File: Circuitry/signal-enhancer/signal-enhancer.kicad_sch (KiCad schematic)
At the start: 25 parts, among them J1 Conn_01x06_Pin, J2 Conn_01x06_Pin, U1 NE555P, U2 74HC14, U4 SN74LS74AN, U5 SN74LS74AN, U7 SN74LS74AN

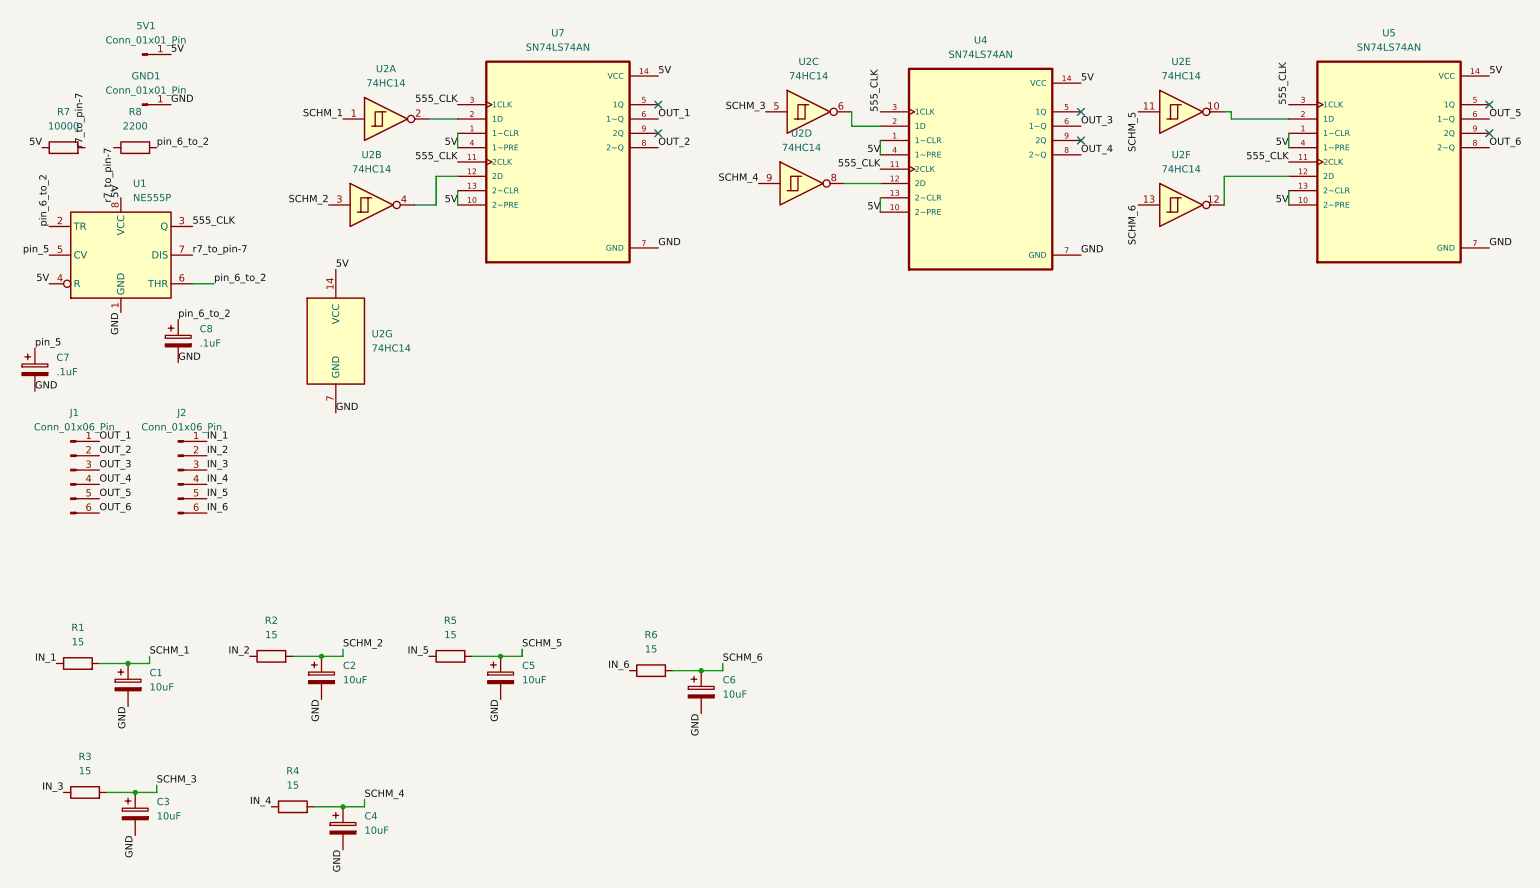
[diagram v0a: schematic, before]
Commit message: Update PCB layout and connector footprints
Modified component values to include Ω symbols and moved value layers to F.SilkS for better visibility. Updated positions of several components and changed connector footprints from 1.27mm to 2.54mm pitch for J2 and related connectors. Added new backup and PCB zip files, removed obsolete autosave and lock files, and added new STL files for valve bracket and holder plate.
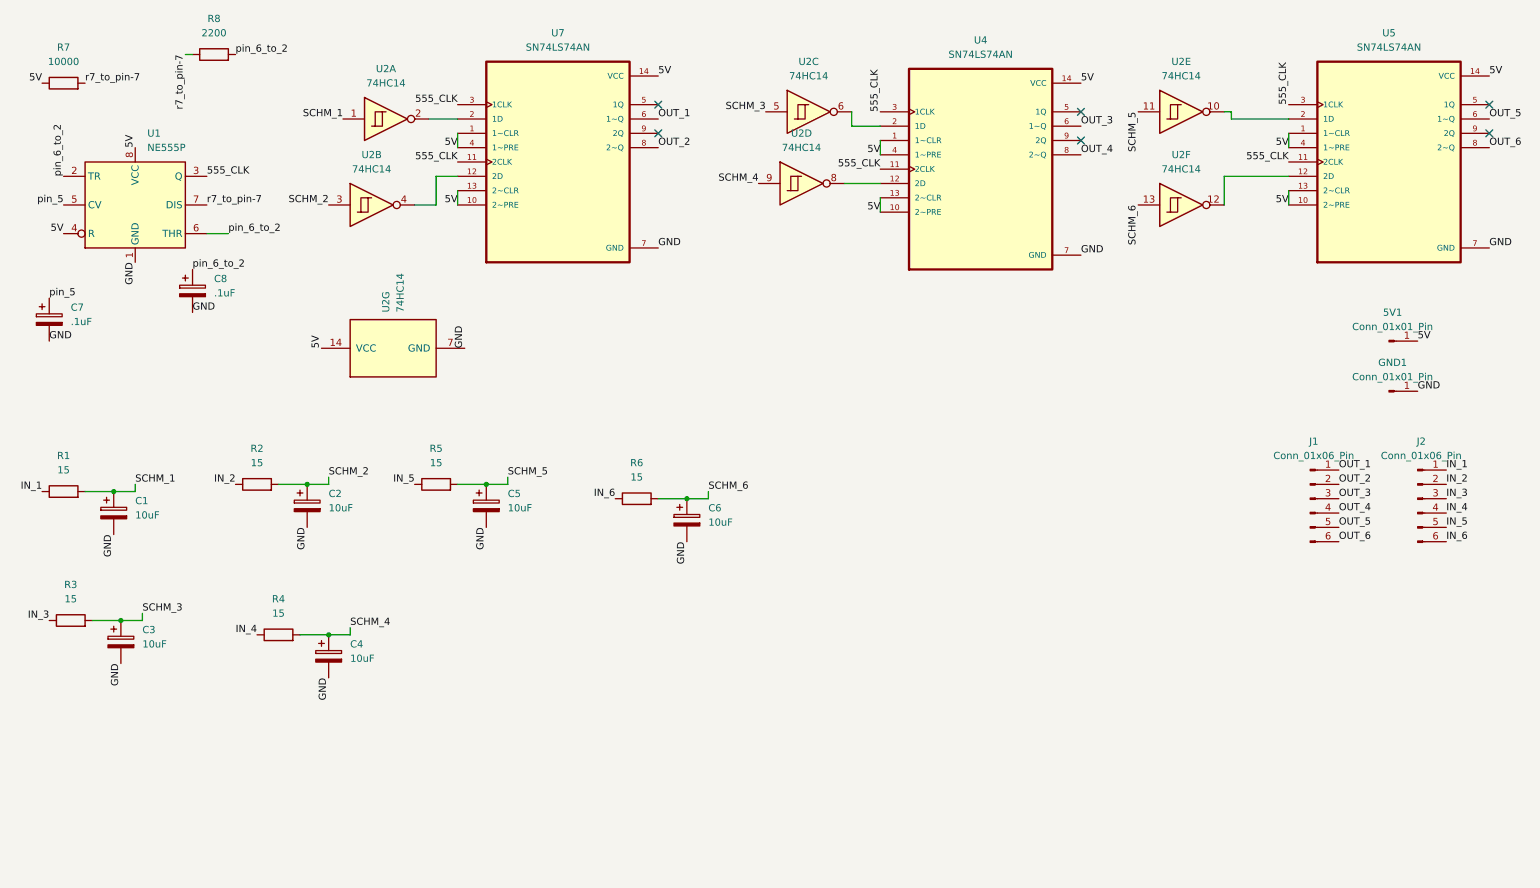
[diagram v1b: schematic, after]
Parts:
- J1, J2: footprint Connector_PinHeader_1.27mm:PinHeader_1x06_P1.27mm_Vertical -> Connector_PinHeader_2.54mm:PinHeader_1x06_P2.54mm_Vertical
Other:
- moved on the sheet: 5V1, C1, C2, C3, C4, C5, C6, C7, C8, GND1, J1, J2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
